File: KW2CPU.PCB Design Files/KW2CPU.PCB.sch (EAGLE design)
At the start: 80 parts, among them IC1 25AA080SN, J1 DF12_M, U1 MKW21D, U3 RF6555, X1 32KHZ, X2 32MHZ

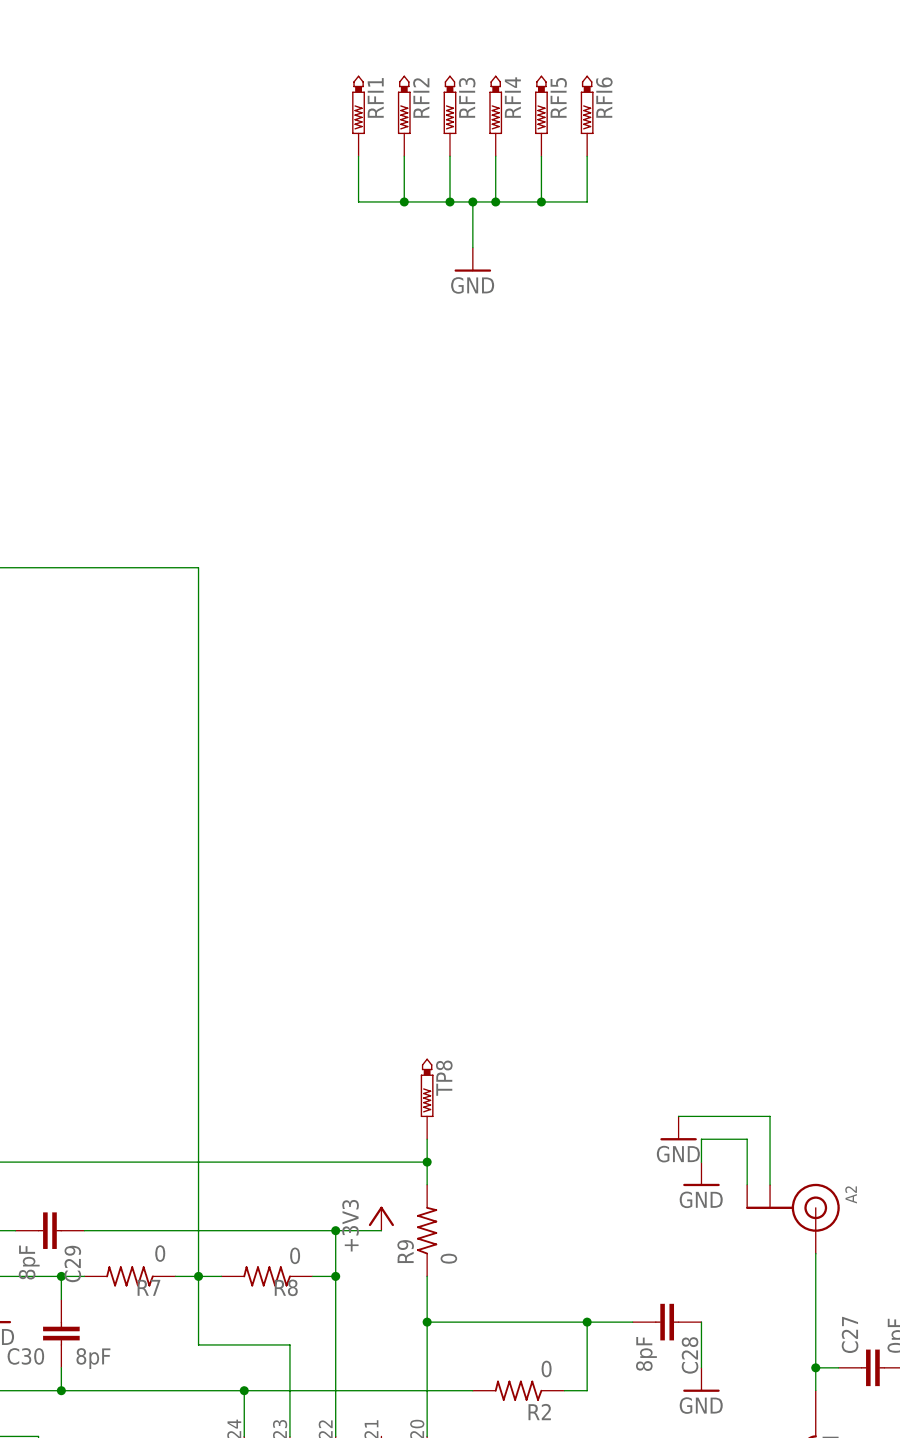
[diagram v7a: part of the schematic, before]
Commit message: Fixes after Rafael's review
* DNP all but the dedicated RX/TX antenna select option via GPIO2.
* DNP all but the LNA passthrough control option.
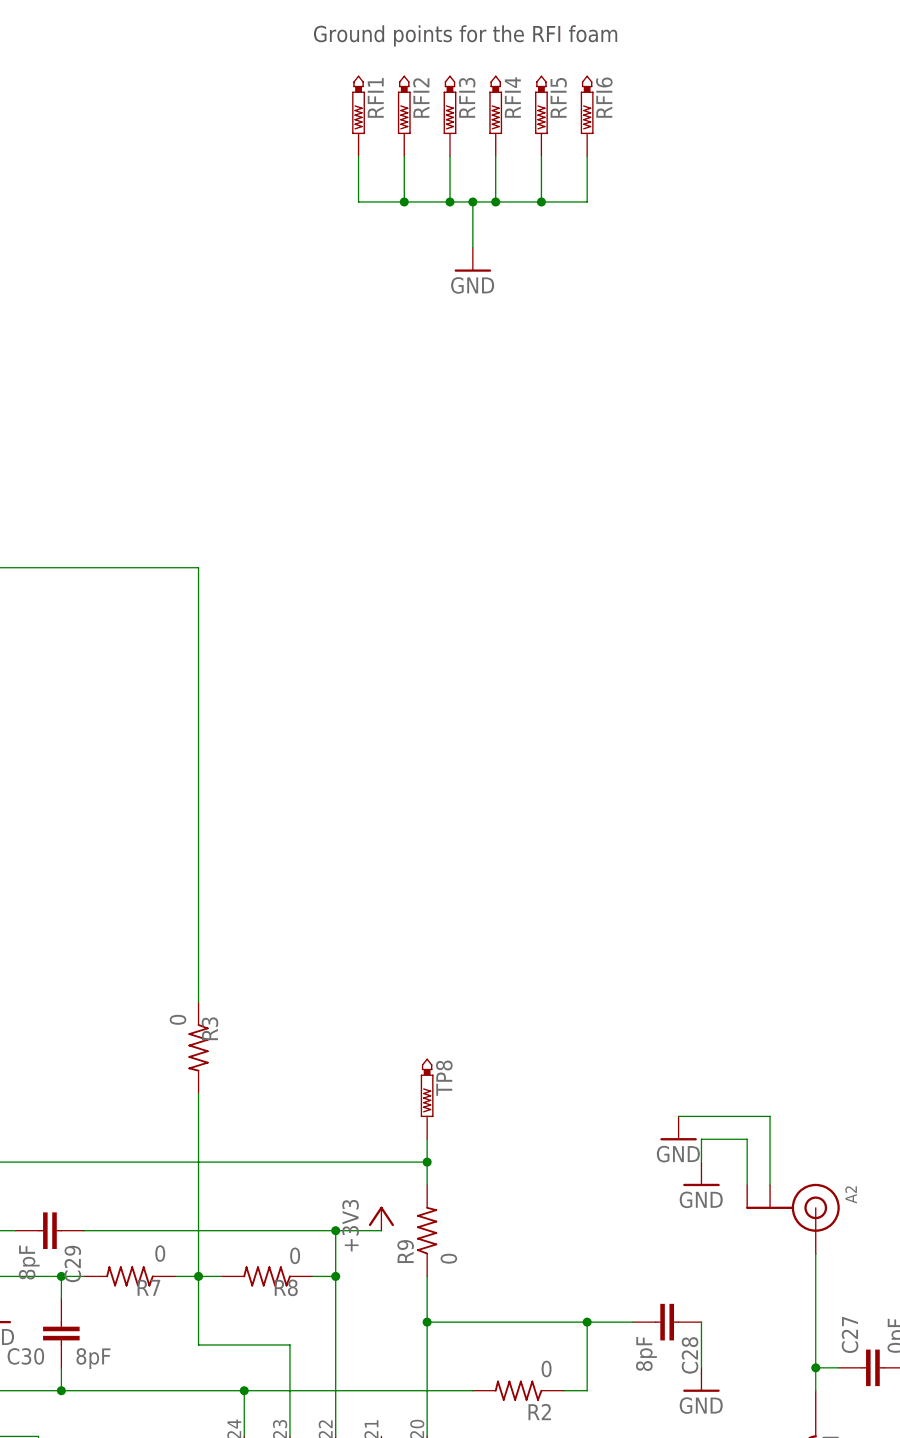
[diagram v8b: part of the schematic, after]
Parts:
- added R3: 0, GW-devices:RF-RRFMD
- R7, R9: NOTES (none) -> DNP
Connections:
- new net N$8: R3.2, R7.1, R8.2, U3.C_LNA
- net GPIO2: now also R3.1; no longer R7.1, R8.2, U3.C_LNA
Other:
- note added: "Ground points for the RFI foam"
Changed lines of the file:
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@@
 <attribute name="MFGN" value="Panasonic"/>
 <attribute name="MFGP" value="ERJ-2GE0R00X"/>
+<attribute name="NOTES" value="DNP"/>
 </part>
 <part name="C28" library="GW-devices" deviceset="RF-C" device="RFMD" value="8pF">
@@
 <attribute name="MFGN" value="Panasonic"/>
 <attribute name="MFGP" value="ERJ-2GE0R00X"/>
+<attribute name="NOTES" value="DNP"/>
 </part>
 <part name="R8" library="GW-devices" deviceset="RF-R" device="RFMD" value="0">
@@
 </part>
 <part name="GND29" library="supply1" deviceset="GND" device=""/>
+<part name="R3" library="GW-devices" deviceset="RF-R" device="RFMD" value="0">
+<attribute name="MFGN" value="Panasonic"/>
+<attribute name="MFGP" value="ERJ-2GE0R00X"/>
+<attribute name="NOTES" value="DNP"/>
+</part>
 </parts>
 <sheets>
 <sheet>
 <plain>
+<text x="337.82" y="172.72" size="1.778" layer="97">Ground points for the RFI foam</text>
 </plain>
 <instances>
@@
 <attribute name="MFGN" x="350.52" y="40.64" size="1.778" layer="96" rot="R90" display="off"/>
 <attribute name="MFGP" x="350.52" y="40.64" size="1.778" layer="96" rot="R90" display="off"/>
+<attribute name="NOTES" x="350.52" y="40.64" size="1.778" layer="96" rot="R90" display="off"/>
 </instance>
 <instance part="C28" gate="G$1" x="378.46" y="30.48" rot="R270">
@@
 <attribute name="NAME" x="321.056" y="35.179" size="1.778" layer="95" rot="R180"/>
 <attribute name="VALUE" x="321.564" y="38.989" size="1.778" layer="96" rot="R180"/>
+<attribute name="NOTES" x="317.5" y="35.56" size="1.778" layer="96" rot="R180" display="off"/>
 </instance>
 <instance part="R8" gate="G$1" x="332.74" y="35.56" smashed="yes" rot="R180">
@@
 </instance>
 <instance part="GND29" gate="1" x="355.6" y="147.32"/>
+<instance part="R3" gate="G$1" x="325.12" y="60.96" smashed="yes" rot="R270">
+<attribute name="MFGN" x="325.12" y="60.96" size="1.778" layer="96" rot="R270" display="off"/>
+<attribute name="MFGP" x="325.12" y="60.96" size="1.778" layer="96" rot="R270" display="off"/>
+<attribute name="NAME" x="325.501" y="64.516" size="1.778" layer="95" rot="R270"/>
+<attribute name="VALUE" x="321.945" y="64.77" size="1.778" layer="96" rot="R270"/>
+<attribute name="NOTES" x="325.12" y="60.96" size="1.778" layer="96" rot="R270" display="off"/>
+</instance>
 </instances>
 <busses>
@@
 <wire x1="-139.7" y1="114.3" x2="243.84" y2="114.3" width="0.1524" layer="91"/>
 <wire x1="243.84" y1="114.3" x2="243.84" y2="99.06" width="0.1524" layer="91"/>
-<pinref part="R7" gate="G$1" pin="1"/>
-<pinref part="R8" gate="G$1" pin="2"/>
-<wire x1="322.58" y1="35.56" x2="325.12" y2="35.56" width="0.1524" layer="91"/>
-<pinref part="U3" gate="G$1" pin="C_LNA"/>
-<wire x1="335.28" y1="17.78" x2="335.28" y2="27.94" width="0.1524" layer="91"/>
-<wire x1="335.28" y1="27.94" x2="325.12" y2="27.94" width="0.1524" layer="91"/>
-<wire x1="325.12" y1="27.94" x2="325.12" y2="35.56" width="0.1524" layer="91"/>
-<wire x1="325.12" y1="35.56" x2="327.66" y2="35.56" width="0.1524" layer="91"/>
-<junction x="325.12" y="35.56"/>
 <wire x1="243.84" y1="114.3" x2="325.12" y2="114.3" width="0.1524" layer="91"/>
-<wire x1="325.12" y1="114.3" x2="325.12" y2="35.56" width="0.1524" layer="91"/>
+<wire x1="325.12" y1="114.3" x2="325.12" y2="68.58" width="0.1524" layer="91"/>
 <junction x="243.84" y="114.3"/>
+<pinref part="R3" gate="G$1" pin="1"/>
+<wire x1="325.12" y1="66.04" x2="325.12" y2="68.58" width="0.1524" layer="91"/>
 </segment>
 </net>
@@
 </segment>
 </net>
+<net name="N$8" class="0">
+<segment>
+<pinref part="R8" gate="G$1" pin="2"/>
+<pinref part="R7" gate="G$1" pin="1"/>
+<wire x1="322.58" y1="35.56" x2="325.12" y2="35.56" width="0.1524" layer="91"/>
+<wire x1="325.12" y1="35.56" x2="327.66" y2="35.56" width="0.1524" layer="91"/>
+<junction x="325.12" y="35.56"/>
+<pinref part="R3" gate="G$1" pin="2"/>
+<wire x1="325.12" y1="55.88" x2="325.12" y2="53.34" width="0.1524" layer="91"/>
+<wire x1="325.12" y1="53.34" x2="325.12" y2="35.56" width="0.1524" layer="91"/>
+<pinref part="U3" gate="G$1" pin="C_LNA"/>
+<wire x1="335.28" y1="17.78" x2="335.28" y2="27.94" width="0.1524" layer="91"/>
+<wire x1="335.28" y1="27.94" x2="325.12" y2="27.94" width="0.1524" layer="91"/>
+<wire x1="325.12" y1="27.94" x2="325.12" y2="35.56" width="0.1524" layer="91"/>
+</segment>
+</net>
